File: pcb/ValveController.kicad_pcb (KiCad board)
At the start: 4 copper layers, 101 parts, among them J10 1770966, J11 1770966, J12 1770966, J13 USB4145-03-0170-C, J14 1990986, J15 1770885, J16 1770885, J2 1990986, J3 1990986, J8 1770966, J9 1770966, Q3 MOC3063S-TA1, Q4 MOC3063S-TA1, Q5 CSD17313Q2, Q6 CPC1017N, Q7 CPC1017N, SW1 TL9320AF400QG, SW3 A6S-1102-H, U1 IRM-03-5, U2 TLV75733P, U5 ESP32-C6-WROOM-1-N4, U6 TPS61040, U7 IS31FL3730, U8 LTV-824S

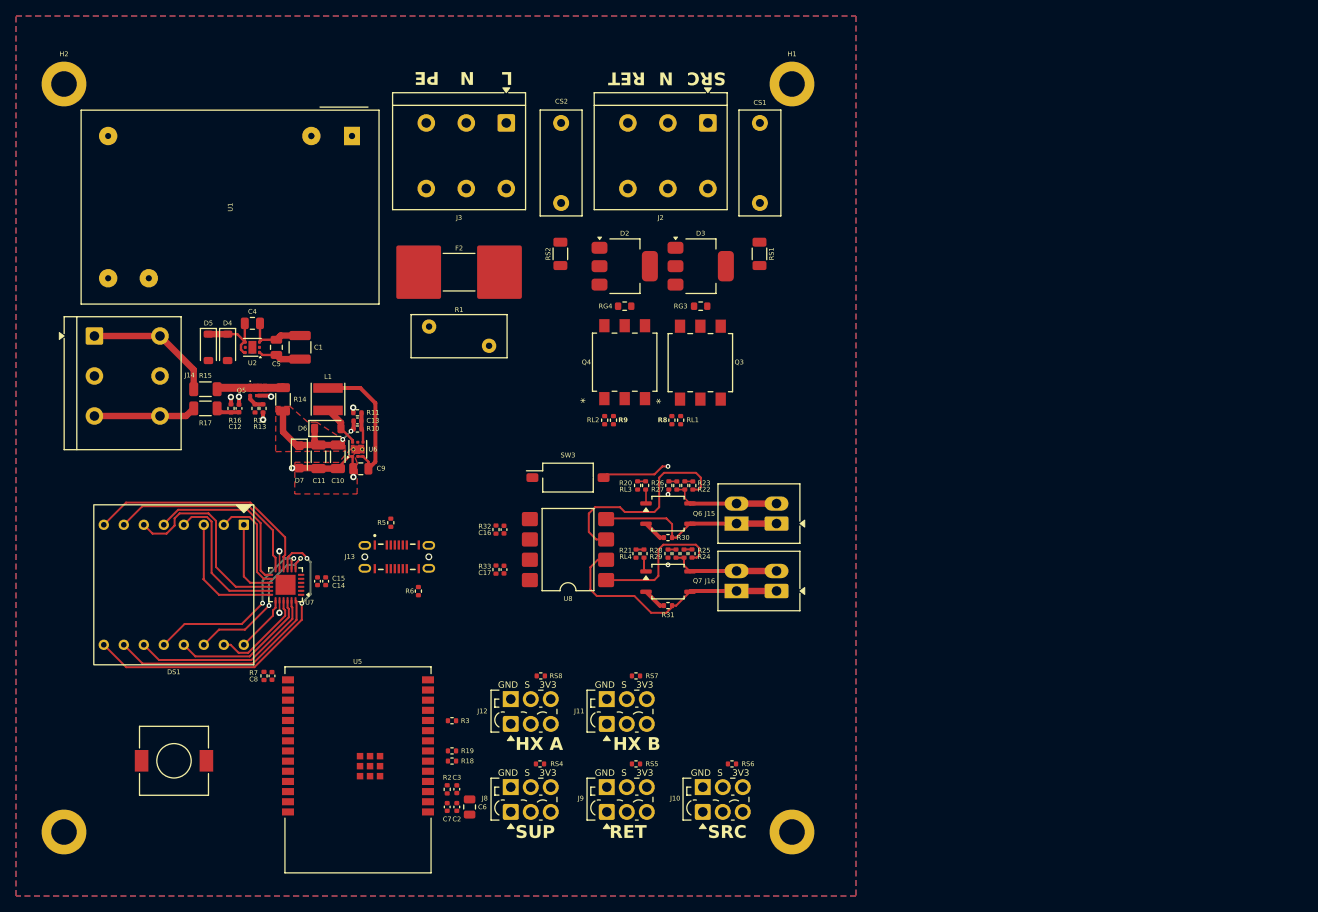
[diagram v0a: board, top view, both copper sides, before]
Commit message: feat(pcb): update schematic and layout, add terminal block footprint, 3D model and datasheets
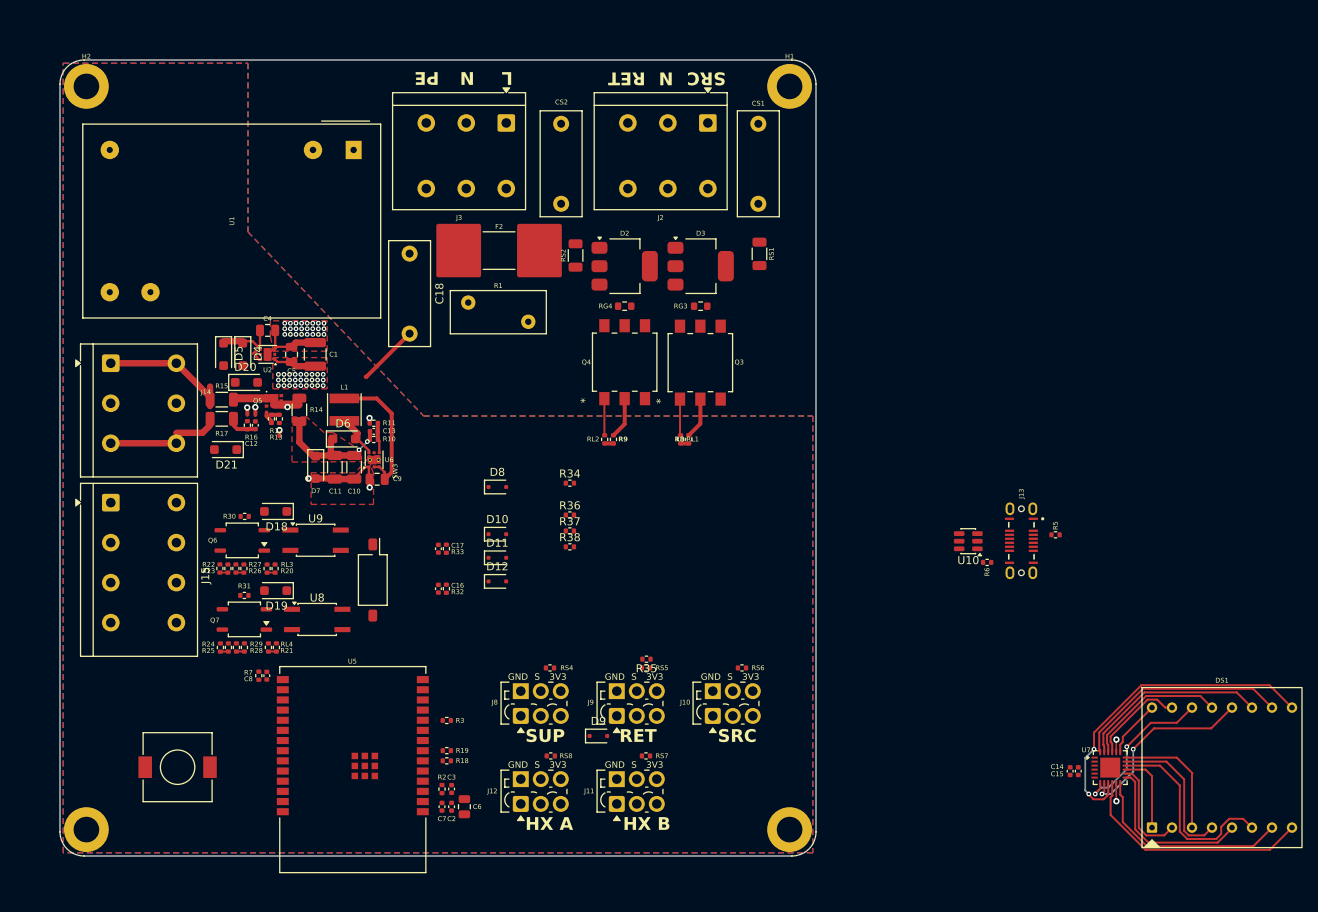
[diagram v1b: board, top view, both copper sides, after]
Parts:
- removed J16: 1770885, TerminalBlock_Phoenix:TerminalBlock_Phoenix_PTSM-0,5-2-2.5-H-THR_1x02_P2.50mm_Horizontal
- added C18: 4.7nF X1/Y2, Capacitor_THT:C_Rect_L13.0mm_W5.0mm_P10.00mm_FKS3_FKP3_MKS4, F.Cu at (104.2, 49.7)
- added D10: PEC3205CS, Diode_SMD:D_SOD-323F, F.Cu at (115.2, 84.8)
- added D11: PEC3205CS, Diode_SMD:D_SOD-323F, F.Cu at (115.2, 87.7)
- added D12: PEC3205CS, Diode_SMD:D_SOD-323F, F.Cu at (115.2, 90.7)
- added D18: SMF51CA, Diode_SMD:D_SOD-123F, F.Cu at (87.5, 81.9)
- added D19: SMF51CA, Diode_SMD:D_SOD-123F, F.Cu at (87.5, 91.8)
- added D20: SMF33A, Diode_SMD:D_SOD-123F, F.Cu at (83.8, 65.8)
- added D21: SMF33A, Diode_SMD:D_SOD-123F, F.Cu at (81.2, 74.2)
- added D8: PEC3205CS, Diode_SMD:D_SOD-323F, F.Cu at (115.2, 78.9)
- added D9: PEC3205CS, Diode_SMD:D_SOD-323F, F.Cu at (127.8, 110.0)
- added R34: 100, Resistor_SMD:R_0402_1005Metric, F.Cu at (124.2, 78.4)
- added R35: 100, Resistor_SMD:R_0402_1005Metric, F.Cu at (133.8, 100.4)
- added R36: 100, Resistor_SMD:R_0402_1005Metric, F.Cu at (124.2, 82.4)
- added R37: 100, Resistor_SMD:R_0402_1005Metric, F.Cu at (124.2, 84.4)
- added R38: 100, Resistor_SMD:R_0402_1005Metric, F.Cu at (124.2, 86.4)
- added U10: USBLC6-2SC6, Package_TO_SOT_SMD:SOT-23-6, F.Cu at (174.0, 85.7)
- added U9: HCPL-354-06AE, Package_SO:SO-4_4.4x3.6mm_P2.54mm, F.Cu at (92.5, 85.5)
- D4, D5: value B5819W -> MBR130LSFT1G; footprint Diode_SMD:D_SOD-123 -> Diode_SMD:D_SOD-123F
- D6: value B5819W -> RB160MM-60TR; footprint Diode_SMD:D_SOD-123 -> Diode_SMD:D_SOD-123F
- J15: value 1770885 -> 1990999; footprint TerminalBlock_Phoenix:TerminalBlock_Phoenix_PTSM-0,5-2-2.5-H-THR_1x02_P2.50mm_Horizontal -> Kleist2:TerminalBlock_Phoenix_SPT-2,5-4-H-5.0_1x04_P5.00mm_Horizontal
- Q6, Q7: value CPC1017N -> CPC1035N
- U8: value LTV-824S -> HCPL-354-06AE; footprint Package_DIP:SMDIP-8_W9.53mm -> Package_SO:SO-4_4.4x3.6mm_P2.54mm
- moved DS1 133.0 mm to (205.8, 114.0), turned to 0 degrees
- moved U7 105.6 mm to (191.8, 114.0), turned to 0 degrees
- moved C14 98.0 mm to (187.8, 114.4), turned to -90 degrees
- moved C15 96.0 mm to (186.8, 114.4), turned to -90 degrees
- moved J15 83.3 mm to (66.8, 80.8), turned to -90 degrees
- moved R5 83.1 mm to (184.9, 84.8), turned to 0 degrees
- moved J13 78.1 mm to (180.7, 85.6), turned to -90 degrees
- moved R6 71.2 mm to (176.4, 88.3), turned to 180 degrees
- moved R25 60.1 mm to (80.5, 98.9), turned to 90 degrees
- moved R23 60.0 mm to (80.5, 89.1), turned to 90 degrees
- moved R24 58.1 mm to (81.5, 98.9), turned to -90 degrees
- moved R22 58.1 mm to (81.5, 89.1), turned to -90 degrees
- moved R29 56.2 mm to (82.5, 98.9), turned to 90 degrees
- moved R27 56.1 mm to (82.5, 89.1), turned to 90 degrees
- moved R28 54.2 mm to (83.5, 98.9), turned to -90 degrees
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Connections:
- H3 pad 1: GND -> unconnected-(H3-Pad1)
- H4 pad 1: GND -> unconnected-(H4-Pad1)
- J10 pad 2: TEMP_SOURCE -> TEMP_SOURCE_CON
- J11 pad 2: TEMP_HX_A -> TEMP_HX_A_CON
- J12 pad 2: TEMP_HX_B -> TEMP_HX_B_CON
- J8 pad 2: TEMP_SUPPLY -> TEMP_SUPPLY_CON
- J9 pad 2: TEMP_RETURN -> TEMP_RETURN_CON
- U5 pad 12: AUX1_DET -> unconnected-(U5-IO11-Pad12)
- U5 pad 16: TEMP_HX_A -> AUX2_EN
- U5 pad 17: TEMP_HX_B -> AUX1_EN
- U5 pad 18: PUMP_PWM -> AUX2_DET
- U5 pad 19: PUMP_FB -> AUX1_DET
- U5 pad 20: AUX1_EN -> PUMP_PWM
- U5 pad 21: AUX2_EN -> PUMP_FB
- U5 pad 24: AUX2_DET -> unconnected-(U5-RXD0-Pad24)
- U5 pad 4: unconnected-(U5-IO4-Pad4) -> TEMP_HX_B
- U5 pad 5: unconnected-(U5-IO5-Pad5) -> TEMP_HX_A
- U8 pad 3: DET1_L -> GND
- U8 pad 4: AUX1_OUT -> AUX2_DET
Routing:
- net AUX2_OUT: track 30.9 -> 0.00 mm
- net DET1_L: track 26.2 -> 0.00 mm
- net AUX1_OUT: track 24.0 -> 0.00 mm
- net WET_24V: track 21.7 -> 0.00 mm, vias 3 -> 0
- net DET2_L: track 17.5 -> 0.00 mm
- net AUX2_IN: track 13.9 -> 0.00 mm
- net AUX1_IN: track 13.8 -> 0.00 mm
- net GND: track 29.4 -> 41.5 mm, vias 6 -> 30
- net U4_A: track 0.00 -> 4.65 mm
- net U3_A: track 0.00 -> 4.55 mm
- net AUX2_DRV: track 1.82 -> 0.00 mm
- net AUX1_DRV: track 1.76 -> 0.00 mm
- net SSR_CLOSE: track 0.00 -> 1.10 mm
- net SSR_OPEN: track 0.00 -> 1.01 mm
- net 3V3: vias 3 -> 30
- added copper zone on F.Cu, net 3V3
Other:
- board outline added: 94.5 x 99.5 mm

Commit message: feat(pcb): complete 4-layer layout — routing, HV isolation rules, EP thermal vias, board art
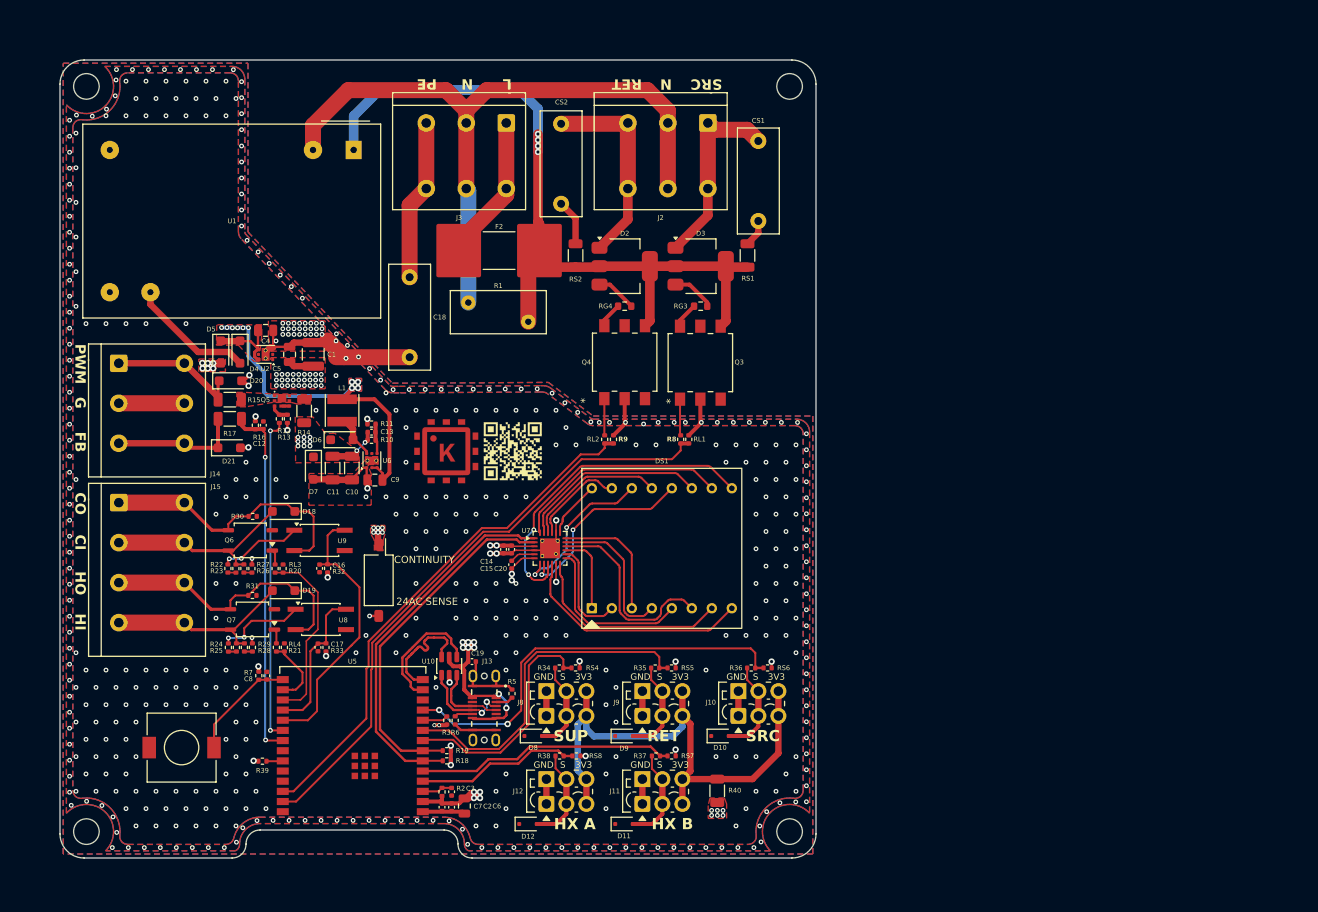
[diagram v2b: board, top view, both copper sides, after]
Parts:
- added ?: , , F.Cu at (122.5, 87.2)
- added ?: , , F.Cu at (122.7, 85.6)
- added ?: , , F.Cu at (120.8, 85.6)
- added ?: , , F.Cu at (120.8, 87.5)
- added ?: , , F.Cu at (86.2, 61.8)
- added ?: , , F.Cu at (86.2, 62.8)
- added C19: 1uF, Capacitor_SMD:C_0402_1005Metric, F.Cu at (112.0, 100.7)
- added C20: 100nF, Capacitor_SMD:C_0402_1005Metric, F.Cu at (117.0, 88.6)
- added G1: KleistLabs_Logo_8mm_Copper, Kleist2:KleistLabs_Logo_8mm_Copper, F.Cu at (108.8, 74.4)
- added G2: QR_HydroMix_SilkOnDark, Kleist2:QR_HydroMix_250um_SilkOnDark, F.Cu at (117.1, 74.4)
- added R39: 10k, Resistor_SMD:R_0402_1005Metric, F.Cu at (85.8, 113.2)
- added R40: 100, Resistor_SMD:R_1206_3216Metric, F.Cu at (142.7, 116.8)
- H1, H2, H3, H4: footprint MountingHole:MountingHole_3.2mm_M3_DIN965_Pad -> MountingHole:MountingHole_3.2mm_M3_ISO7380
- RL3, RL4: value 680 -> 470
- moved C14 76.1 mm to (117.0, 86.7)
- moved C15 76.1 mm to (115.9, 86.7)
- moved DS1 75.2 mm to (135.7, 86.5)
- moved U7 75.2 mm to (121.8, 86.5)
- moved R5 70.8 mm to (117.0, 104.7), turned to 90 degrees
- moved J13 70.3 mm to (113.5, 106.5)
- moved R6 69.4 mm to (109.9, 108.0), turned to -90 degrees
- moved U10 66.7 mm to (109.2, 101.3), turned to 90 degrees
- moved D10 37.6 mm to (143.0, 110.0)
- moved D11 36.8 mm to (131.0, 121.0)
- moved D8 31.4 mm to (119.7, 110.0)
- moved D12 30.6 mm to (119.0, 121.0)
- moved R37 30.1 mm to (135.0, 112.5), turned to 180 degrees
- moved R36 29.7 mm to (146.9, 101.5), turned to 180 degrees
- moved R38 26.2 mm to (123.0, 112.5), turned to 180 degrees
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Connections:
- D20 pad 1: GND -> PUMP_PWM_OUT
- D20 pad 2: PUMP_PWM_OUT -> GND
- D21 pad 1: GND -> PUMP_FB_IN
- D21 pad 2: PUMP_FB_IN -> GND
- J10 pad 3: 3V3 -> 3V3_PROBES
- J11 pad 3: 3V3 -> 3V3_PROBES
- J12 pad 3: 3V3 -> 3V3_PROBES
- J8 pad 3: 3V3 -> 3V3_PROBES
- J9 pad 3: 3V3 -> 3V3_PROBES
- U5 pad 23: unconnected-(U5-IO15-Pad23) -> IO15
- U7 pad 5: GND -> C_FILT
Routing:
- net MAINS_L_F: track 0.00 -> 101.6 mm, vias 0 -> 4
- net MAINS_N: track 0.00 -> 86.3 mm
- net VBUS: track 0.00 -> 84.7 mm, vias 0 -> 14
- net SSR_OPEN: track 1.01 -> 75.9 mm
- net 3V3_PROBES: track 0.00 -> 66.9 mm
- net GND: track 41.5 -> 107.8 mm, vias 30 -> 464
- net SSR_CLOSE: track 1.10 -> 65.2 mm
- net TEMP_SOURCE: track 0.00 -> 52.9 mm, vias 0 -> 2
- net I2C_SDA: track 0.00 -> 46.4 mm
- net I2C_SCL: track 0.00 -> 44.3 mm
- net TEMP_RETURN: track 0.00 -> 42.6 mm
- net PUMP_FB: track 2.94 -> 44.1 mm, vias 0 -> 2
- net PUMP_PWM: track 0.00 -> 40.9 mm, vias 0 -> 2
- net AUX1_DET: track 0.00 -> 34.6 mm
- net AUX1_OUT: track 0.00 -> 34.6 mm
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- added copper zone on B.Cu, net 5V
- added copper zone on F.Cu, net 5V
- added copper zone on In1.Cu, net 5V
- added copper zone on In2.Cu, net 5V
- added copper zone on F.Cu, net PUMP_PWM_LINE
- added copper zone on F.Cu, net VBUS
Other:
- board size 94.5 x 99.5 mm -> 94.5 x 99.8 mm
- board text added: "24AC SENSE"
- board text added: "CI"
- board text added: "CO"
- board text added: "CONTINUITY"
- board text added: "FB"
- board text added: "G"
- board text added: "HI"
- board text added: "HO"
- board text added: "PWM"
- board text added: "{ "ViaStitching": "0.2", "stitch_zone_0": { "HSpacing": "1", "VSpacing": "1", "HOffset": "0", "VOffset": "0", "Clearance": "0", "Randomize": false } }"
- board text added: "{ "ViaStitching": "0.2", "stitch_zone_0": { "HSpacing": "2", "VSpacing": "2", "HOffset": "0", "VOffset": "0", "Clearance": "0", "Randomize": false } }"
